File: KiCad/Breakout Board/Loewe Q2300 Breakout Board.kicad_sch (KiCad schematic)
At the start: 2 parts, among them J1 VGA DSUB-15, J2 JST_XH_1x10_P2.50mm_Horizontal

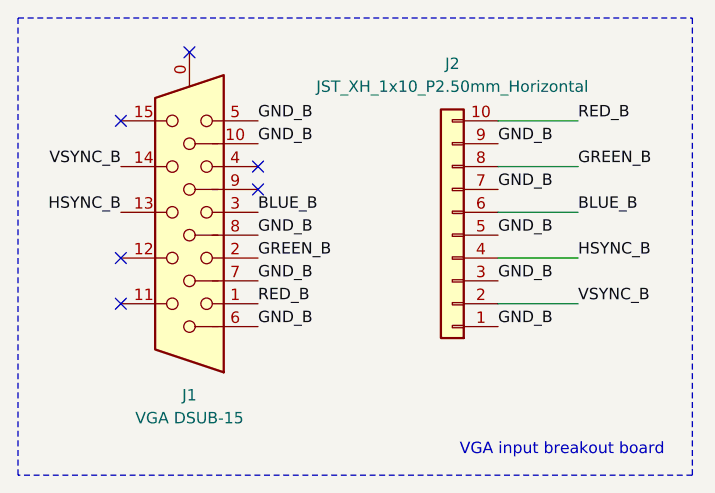
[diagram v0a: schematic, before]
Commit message: Replace JST XH 2.50 mm with custom 2.54 mm.
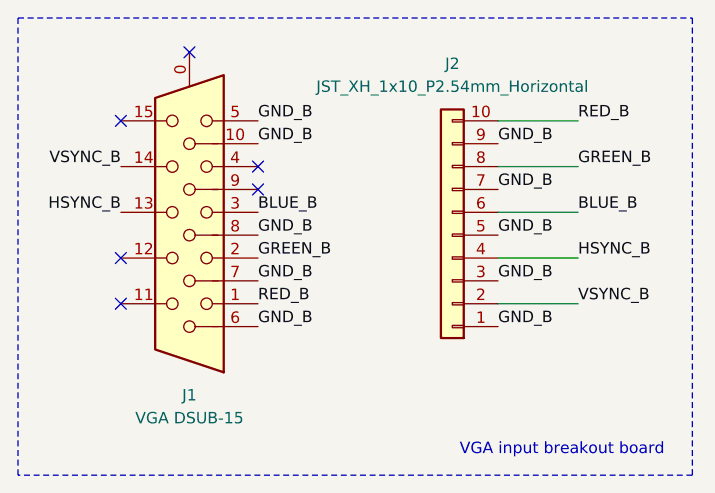
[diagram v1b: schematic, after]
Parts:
- J2: value JST_XH_1x10_P2.50mm_Horizontal -> JST_XH_1x10_P2.54mm_Horizontal; footprint Connector_JST:JST_XH_S10B-XH-A_1x10_P2.50mm_Horizontal -> JST_XH_S10B_2.54mm:JST_XH_S10B-XH-A_1x10_P2.54mm_Horizontal
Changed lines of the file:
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@@
 			)
 		)
-		(property "Value" "JST_XH_1x10_P2.50mm_Horizontal"
+		(property "Value" "JST_XH_1x10_P2.54mm_Horizontal"
 			(at 68.58 26.67 0)
 			(effects
@@
 			)
 		)
-		(property "Footprint" "Connector_JST:JST_XH_S10B-XH-A_1x10_P2.50mm_Horizontal"
+		(property "Footprint" "JST_XH_S10B_2.54mm:JST_XH_S10B-XH-A_1x10_P2.54mm_Horizontal"
 			(at 68.58 43.18 0)
 			(effects
@@
 		)
 		(instances
-			(project "Loewe Q2300 Breakout"
+			(project "Loewe Q2300 Breakout Board"
 				(path "/027c2a37-84fa-4fcd-bb4d-5ec742c0cf3f"
 					(reference "J2")
@@
 		)
 		(instances
-			(project "Loewe Q2300 Breakout"
+			(project "Loewe Q2300 Breakout Board"
 				(path "/027c2a37-84fa-4fcd-bb4d-5ec742c0cf3f"
 					(reference "J1")

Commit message: Replace incorrect Connector_Dsub:DSUB-15-HD_Male with Connector_Dsub:DSUB-15-HD_Female.
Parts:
- J1: footprint Connector_Dsub:DSUB-15-HD_Male_Horizontal_P2.29x1.98mm_EdgePinOffset3.03mm_Housed_MountingHolesOffset4.94mm -> Connector_Dsub:DSUB-15-HD_Female_Horizontal_P2.29x1.98mm_EdgePinOffset3.03mm_Housed_MountingHolesOffset4.94mm
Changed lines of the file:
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@@
 			)
 		)
-		(property "Footprint" "Connector_Dsub:DSUB-15-HD_Male_Horizontal_P2.29x1.98mm_EdgePinOffset3.03mm_Housed_MountingHolesOffset4.94mm"
+		(property "Footprint" "Connector_Dsub:DSUB-15-HD_Female_Horizontal_P2.29x1.98mm_EdgePinOffset3.03mm_Housed_MountingHolesOffset4.94mm"
 			(at 63.5 50.8 0)
 			(effects
